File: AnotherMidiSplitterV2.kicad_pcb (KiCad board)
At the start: 2 copper layers, 65 x 98 mm, 44 parts, among them J1 IN, J10 OUT, J11 OUT, J2 USB_power, J4 OUT, J5 OUT, J6 OUT, J7 OUT, J8 OUT, J9 OUT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

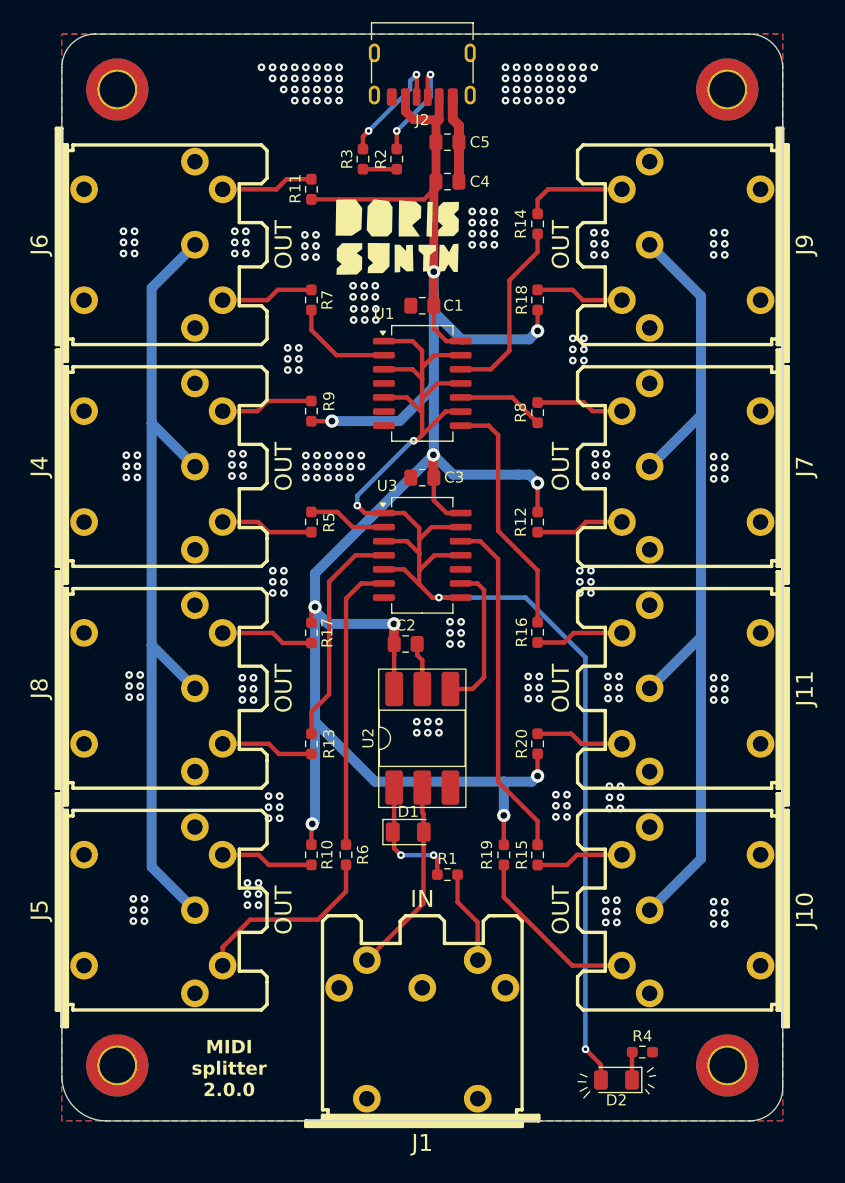
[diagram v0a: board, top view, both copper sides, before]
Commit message: add resistor to optoisolator
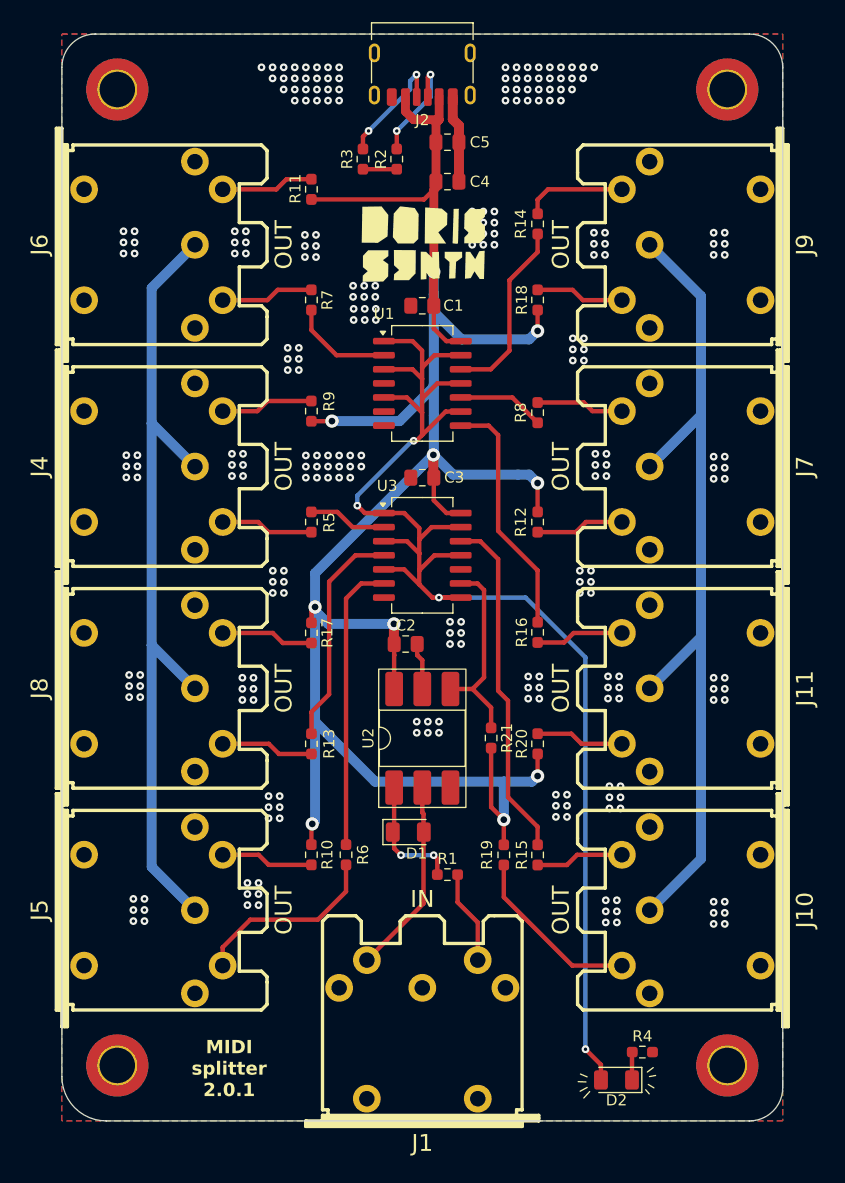
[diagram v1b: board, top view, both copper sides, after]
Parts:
- added R21: 470, Resistor_SMD:R_0603_1608Metric_Pad0.98x0.95mm_HandSolder, F.Cu at (179.7, 101.5)
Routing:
- net +5V: track 188.2 -> 195.2 mm
- net Net-(R21-Pad1): track 13.7 -> 17.9 mm
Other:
- board text added: "MIDI splitter 2.0.1"
- board text removed: "MIDI splitter 2.0.0"

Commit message: Update Variables
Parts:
- added D3: PWR LED, LED_SMD:LED_1206_3216Metric, F.Cu at (183.5, 39.5)
- added D4: PWR LED, LED_THT:LED_D3.0mm_Horizontal_O1.27mm_Z2.0mm, F.Cu at (164.8, 44.8)
- added R22: 470, Resistor_SMD:R_0603_1608Metric_Pad0.98x0.95mm_HandSolder, F.Cu at (183.5, 41.9)
- added R23: 470, Resistor_SMD:R_0603_1608Metric_Pad0.98x0.95mm_HandSolder, F.Cu at (163.8, 47.5)
- moved R16 10.1 mm to (183.9, 102.0)
- moved R20 10.1 mm to (183.9, 91.9), turned to -90 degrees
- moved R5 10.0 mm to (163.5, 72.0), turned to -90 degrees
- moved R17 10.0 mm to (163.5, 102.0)
- moved R9 9.99 mm to (163.5, 82.0)
- moved R7 9.96 mm to (163.5, 52.0)
- moved R13 9.95 mm to (163.5, 92.0)
- moved R11 9.93 mm to (163.5, 61.9)
- moved R12 9.86 mm to (183.9, 72.1), turned to 90 degrees
- moved R8 9.86 mm to (183.9, 82.0), turned to 90 degrees
- moved R14 6.86 mm to (183.9, 62.0)
- moved R18 6.86 mm to (183.9, 55.1)
- moved R6 3.18 mm to (163.4, 112.0)
- moved R10 3.12 mm to (166.6, 112.0)
- moved R15 3.05 mm to (180.8, 112.0)
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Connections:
- R10 pad 2: Net-(J5-Pad5) -> Net-(J5-Pad4)
- R11 pad 2: Net-(J6-Pad5) -> Net-(J6-Pad4)
- R12 pad 2: Net-(J7-Pad5) -> Net-(J7-Pad4)
- R13 pad 1: Net-(J8-Pad4) -> Net-(J8-Pad5)
- R14 pad 1: Net-(J9-Pad4) -> Net-(J9-Pad5)
- R15 pad 1: Net-(J10-Pad4) -> Net-(J10-Pad5)
- R16 pad 1: Net-(J11-Pad4) -> Net-(J11-Pad5)
- R17 pad 2: Net-(J8-Pad5) -> Net-(J8-Pad4)
- R18 pad 2: Net-(J9-Pad5) -> Net-(J9-Pad4)
- R19 pad 2: Net-(J10-Pad5) -> Net-(J10-Pad4)
- R20 pad 2: Net-(J11-Pad5) -> Net-(J11-Pad4)
- R5 pad 1: Net-(J4-Pad4) -> Net-(J4-Pad5)
- R6 pad 1: Net-(J5-Pad4) -> Net-(J5-Pad5)
- R7 pad 1: Net-(J6-Pad4) -> Net-(J6-Pad5)
- R8 pad 1: Net-(J7-Pad4) -> Net-(J7-Pad5)
- R9 pad 2: Net-(J4-Pad5) -> Net-(J4-Pad4)
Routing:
- net +5V: track 195.2 -> 229.2 mm, vias 10 -> 11
- net Net-(R16-Pad2): track 22.1 -> 32.0 mm
- net Net-(R13-Pad2): track 20.3 -> 11.3 mm
- net Net-(R7-Pad2): track 9.28 -> 18.2 mm
- net /MIDI_SIG: track 128.3 -> 135.5 mm
- net Net-(R5-Pad2): track 7.11 -> 13.9 mm
- net Net-(R8-Pad2): track 7.88 -> 14.4 mm
- net Net-(R14-Pad2): track 16.7 -> 10.7 mm
- net Net-(D4-K): track 0.00 -> 2.67 mm
- net Net-(D3-K): track 0.00 -> 2.61 mm
- net Net-(R21-Pad1): track 17.9 -> 15.7 mm
- net GND: track 169.3 -> 171.2 mm, vias 259 -> 273
- net Net-(D2-K): track 2.52 -> 4.37 mm
- net Net-(R15-Pad2): track 31.3 -> 29.9 mm
- net Net-(R6-Pad2): track 26.2 -> 27.3 mm
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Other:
- board text added: "${ProjectTitle} ${Revision} ${Company} ${CURRENT_DATE}"
- board text added: "MIDI DATA"
- board text added: "PWR"
- board text removed: "MIDI splitter 2.0.1"
